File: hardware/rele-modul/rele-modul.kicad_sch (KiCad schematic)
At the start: 40 parts, among them J100 24V IN, J101 RELÉ 1, J102 RELÉ 2, J103 RELÉ 3, J104 RELÉ 4, J105 SCT-013, K1 RTD14024, K2 RTD14024, K3 RTD14024, K4 RTD14024, Q100 IRFR120N, U101 ULN2803ADWR

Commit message: Hardver: legolcsóbb beszerzés (D84) – Hestore + DigiKey, a rajz a kapható típusokra igazítva; beszerzési lista
- gen/beszerzes.py → bom/beszerzes.csv: BOM-tételenként forrás, Hestore-kód, nettó ár, készlet
- J1/J100 Degson DG250, J201 DG128 (15 A), J202–J204 KF128, F201 15 A; L1/L3 HPI0630 (saját footprint);
  R209 CRE2512; C40/C41 12 pF; ESP32-C6-WROOM-1-N8; SS56C, BAT54HT1G, STPS3L60U, BLM18EG221
- NYÁK-ok újragenerálva (a layout még nem indult el); bekötés változatlan, ellenorzes.py: 0 hiba
- SAMPLE-KERESEK: az NTMFS5C604NL nincs kézben (javítva)

Co-Authored-By: Claude Opus 5.5 <noreply@anthropic.com>
Claude-Session: https://claude.ai/code/session_01KVtZMUPbtveTXy9VyJshyt
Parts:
- J100: footprint TerminalBlock_Phoenix:TerminalBlock_Phoenix_PT-1,5-2-5.0-H_1x02_P5.00mm_Horizontal -> TerminalBlock_Degson:TerminalBlock_Degson_DG250-3.5-02P_1x02_P3.50mm_45Degree; Megjegyzés push-in, a típus a DIN-ház vállától függ (D50) -> D84: Degson DG250-3.5-02P – rugós, nyomógombos, 8 A (UL), 0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
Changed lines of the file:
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@@
 			)
 		)
-		(property "Footprint" "TerminalBlock_Phoenix:TerminalBlock_Phoenix_PT-1,5-2-5.0-H_1x02_P5.00mm_Horizontal"
+		(property "Footprint" "TerminalBlock_Degson:TerminalBlock_Degson_DG250-3.5-02P_1x02_P3.50mm_45Degree"
 			(at 33.02 69.85 0)
 			(hide yes)
@@
 			)
 		)
-		(property "Megjegyzés" "push-in, a típus a DIN-ház vállától függ (D50)"
+		(property "Megjegyzés" "D84: Degson DG250-3.5-02P – rugós, nyomógombos, 8 A (UL), 0,2–1,5 mm²"
 			(at 33.02 69.85 0)
 			(hide yes)

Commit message: Hardver: legolcsóbb beszerzés LCSC-ről (D85), megszűnt FET-ek pótlása, LCSC-kosárlista
- gen/lcsc.py: LCSC-árak a JLC alkatrészkeresőjéből; gen/beszerzes.py soronként a legolcsóbb forrás (Hestore / LCSC, ÁFA-val)
- bom/lcsc-kosar.csv: 99 tétel (~15 eFt), az LCSC BOM Tooljába feltölthető; házak később, ST-Link/Nucleo kézben
- Q202–Q207 NTD5C648NL → NCE6080K, Q201 NTMFS5C604NL → NCEP6090AGU (nem kaphatók), F201 → NANO² 15 A,
  D211–D216 SS56B, J1/J100 DG128, L1/L3 LCSC-s 0630-as tekercs, kis ESR-ű kvarcok
- bekötés változatlan (netlista 0 / 0), ellenorzes.py: 0 hiba

Co-Authored-By: Claude Opus 5.5 <noreply@anthropic.com>
Claude-Session: https://claude.ai/code/session_01KVtZMUPbtveTXy9VyJshyt
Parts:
- J100: footprint TerminalBlock_Degson:TerminalBlock_Degson_DG250-3.5-02P_1x02_P3.50mm_45Degree -> TerminalBlock_Phoenix:TerminalBlock_Phoenix_MKDS-1,5-2_1x02_P5.00mm_Horizontal; Megjegyzés D84: Degson DG250-3.5-02P – rugós, nyomógombos, 8 A (UL), 0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 -> D85: Degson DG128-5.0-02P – csavaros, 5,0 mm, 15 A (UL), 2,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
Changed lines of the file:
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@@
 			)
 		)
-		(property "Footprint" "TerminalBlock_Degson:TerminalBlock_Degson_DG250-3.5-02P_1x02_P3.50mm_45Degree"
+		(property "Footprint" "TerminalBlock_Phoenix:TerminalBlock_Phoenix_MKDS-1,5-2_1x02_P5.00mm_Horizontal"
 			(at 33.02 69.85 0)
 			(hide yes)
@@
 			)
 		)
-		(property "Megjegyzés" "D84: Degson DG250-3.5-02P – rugós, nyomógombos, 8 A (UL), 0,2–1,5 mm²"
+		(property "Megjegyzés" "D85: Degson DG128-5.0-02P – csavaros, 5,0 mm, 15 A (UL), 2,5 mm²"
 			(at 33.02 69.85 0)
 			(hide yes)

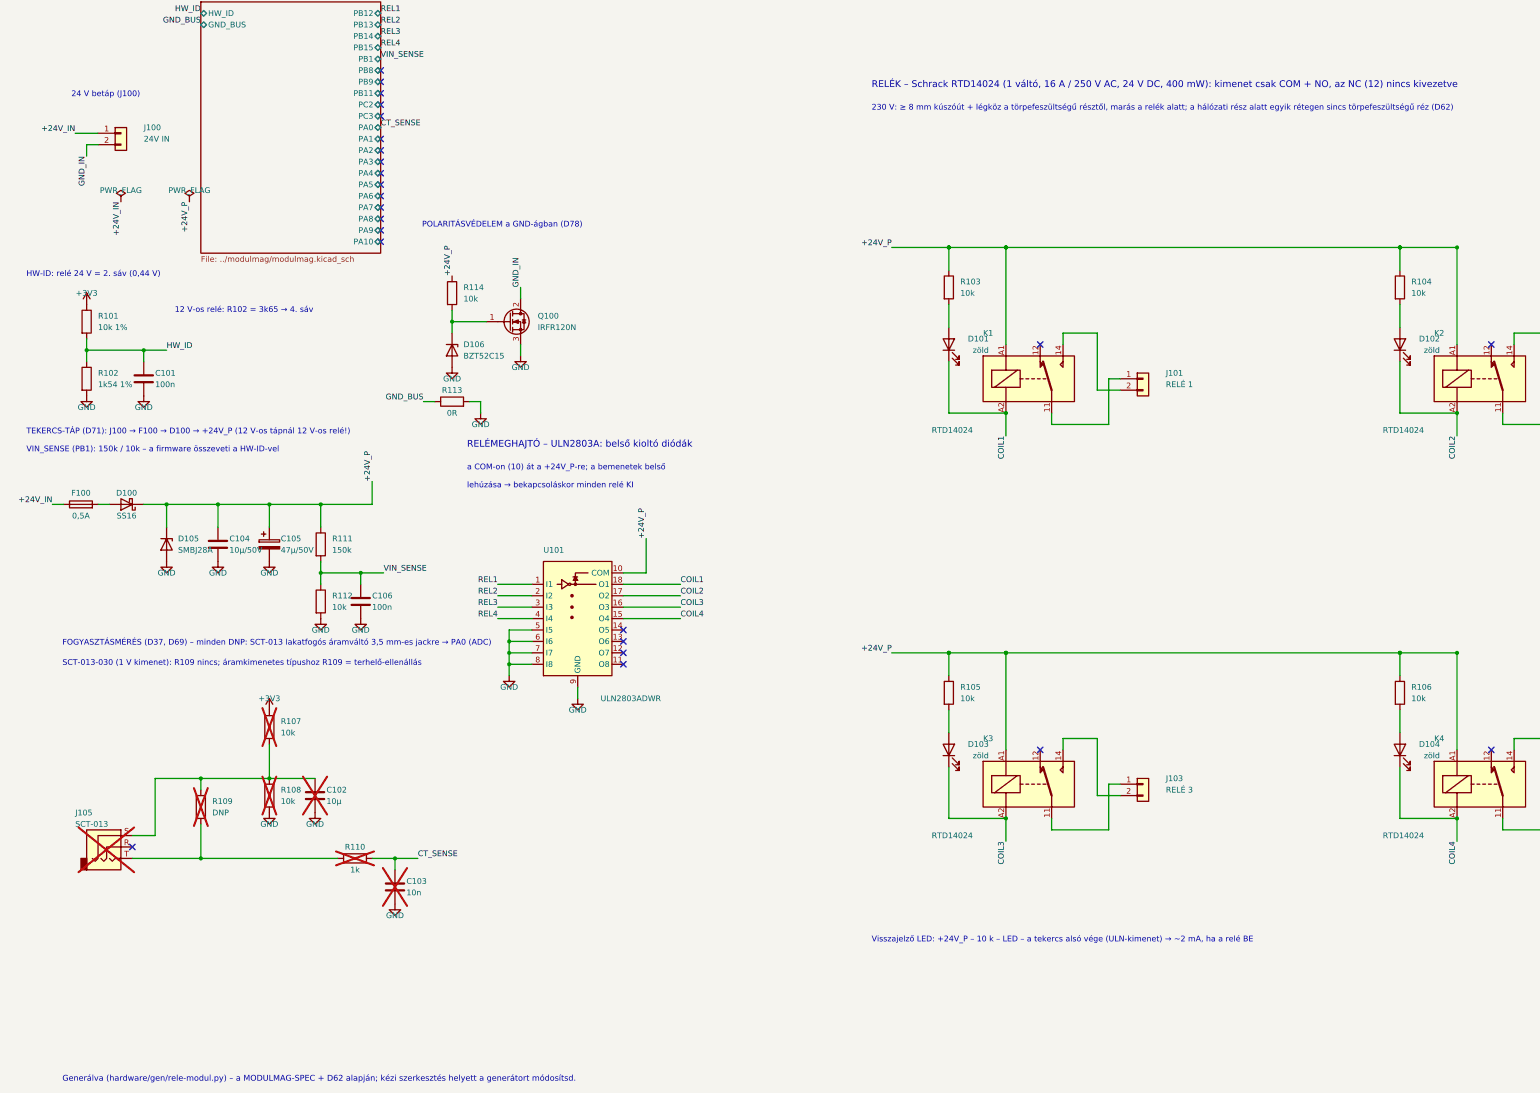
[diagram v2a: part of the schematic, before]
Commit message: Hardver: kézzel átrendezett kapcsolási rajzok (D67), védelem a generátor felülírása ellen; rajzdátum 10-23
- mind az öt lap kézi szerkesztésű – gen/kezi-lapok.txt; a build.sh ezeket nem generálja újra, csak ellenőrzi (felülírás: --force)
- bekötés változatlan (netlista 0 / 0), ERC rendben, ellenorzes.py: 0 hiba
- komponenslista: állapot 10-23

Co-Authored-By: Claude Opus 5.5 <noreply@anthropic.com>
Claude-Session: https://claude.ai/code/session_01KVtZMUPbtveTXy9VyJshyt
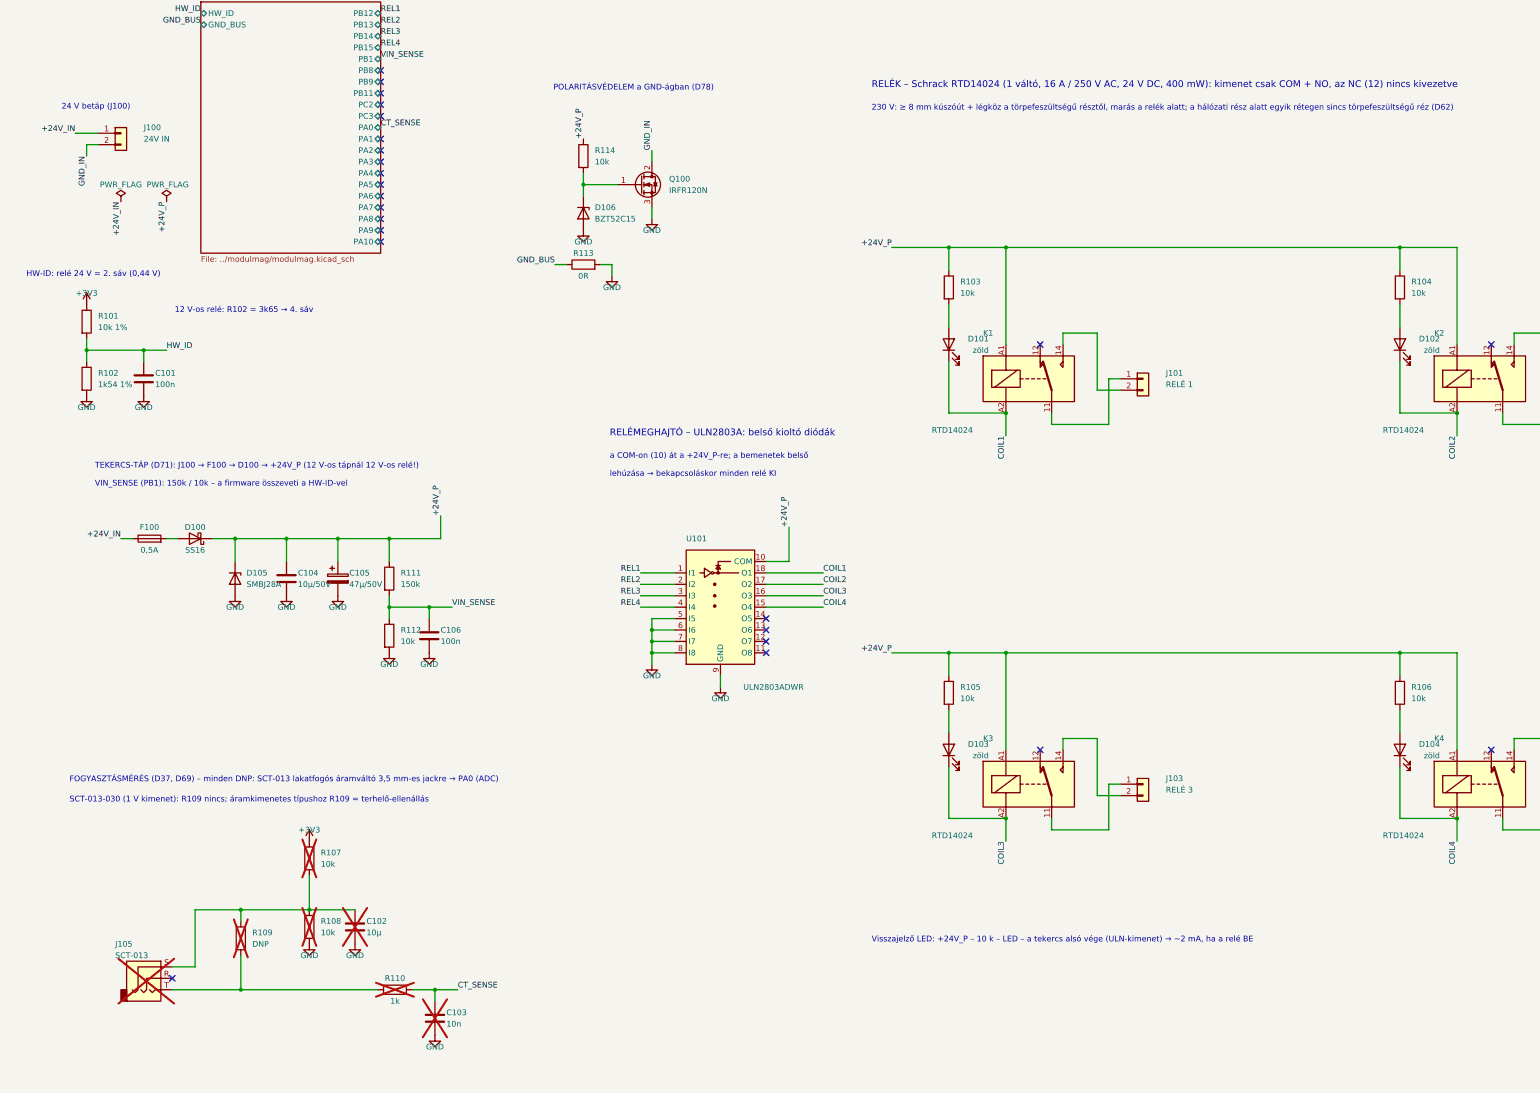
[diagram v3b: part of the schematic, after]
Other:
- note removed: "Generálva (hardware/gen/rele-modul.py) – a MODULMAG-SPEC + D62 alapján; kézi szerkesztés helyett a generátort módosítsd."
- moved on the sheet: C102, C103, C104, C105, C106, D100, D105, D106, F100, J105, Q100, R107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
